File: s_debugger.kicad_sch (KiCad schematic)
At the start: 34 parts, among them J4 USB_C_Receptacle, Q1 S9013, U2 XC6206PxxxMR

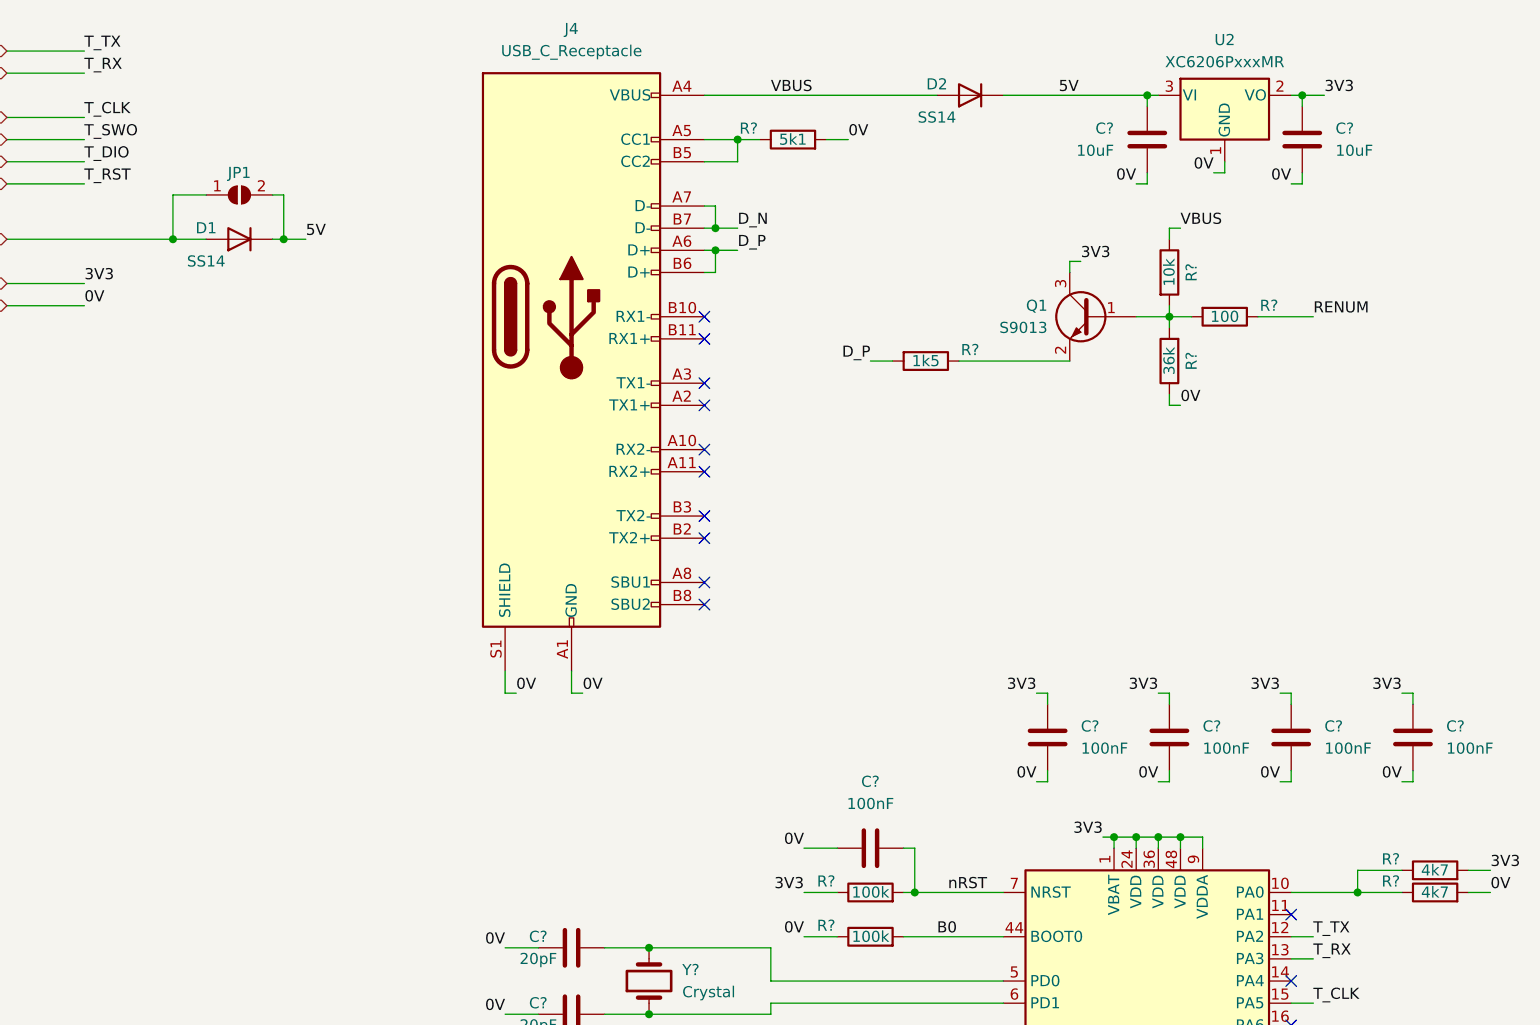
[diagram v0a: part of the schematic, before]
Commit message: passif en 0402
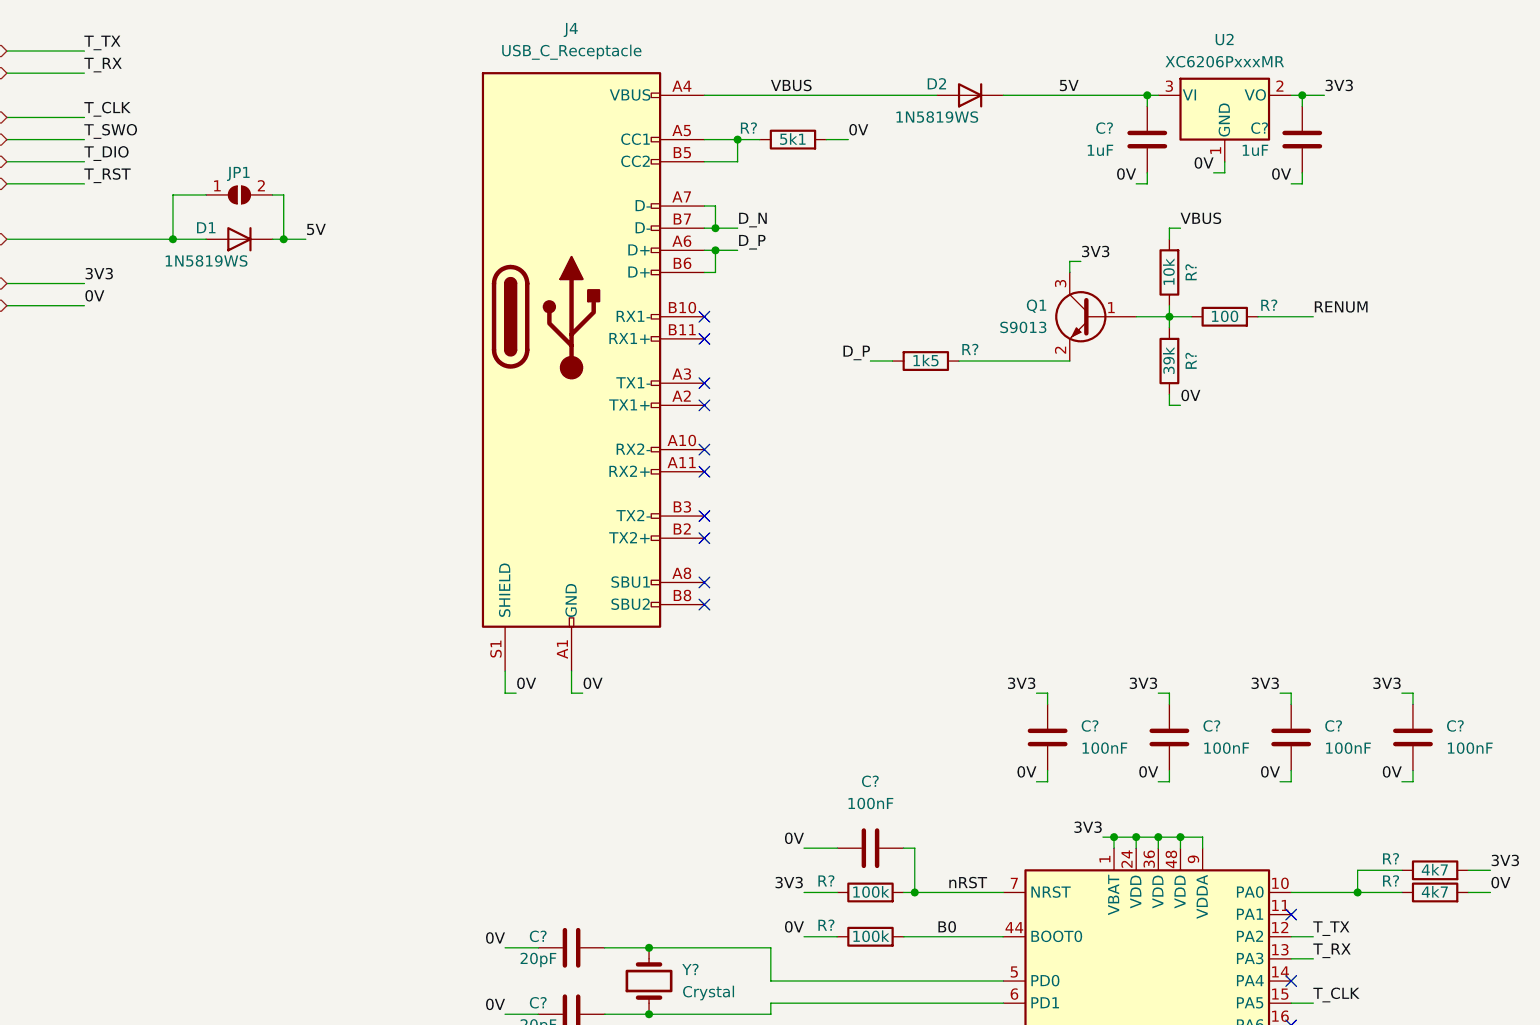
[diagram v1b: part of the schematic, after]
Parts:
- removed C? (x5): 100nF, Capacitor_SMD:C_0603_1608Metric, symbol Device:C
- removed C?: 10uF, Capacitor_SMD:C_0805_2012Metric, symbol Device:C
- removed C?: 20pF, Capacitor_SMD:C_0603_1608Metric, symbol Device:C
- removed R? (x2): 100k, Resistor_SMD:R_0603_1608Metric, symbol Device:R
- removed R? (x2): 10k, Resistor_SMD:R_0603_1608Metric, symbol Device:R
- removed R?: 100, Resistor_SMD:R_0603_1608Metric, symbol Device:R
- removed R?: 4k7, Resistor_SMD:R_0603_1608Metric, symbol Device:R
- added C? (x5): 100nF, Capacitor_SMD:C_0402_1005Metric, symbol Device:C
- added C?: 1uF, Capacitor_SMD:C_0402_1005Metric, symbol Device:C
- added C?: 20pF, Capacitor_SMD:C_0402_1005Metric, symbol Device:C
- added R? (x2): 10k, Resistor_SMD:R_0402_1005Metric, symbol Device:R
- added R? (x2): 100k, Resistor_SMD:R_0402_1005Metric, symbol Device:R
- added R?: 4k7, Resistor_SMD:R_0402_1005Metric, symbol Device:R
- added R?: 100, Resistor_SMD:R_0402_1005Metric, symbol Device:R
- C?: value 10uF -> 1uF; footprint Capacitor_SMD:C_0805_2012Metric -> Capacitor_SMD:C_0402_1005Metric; LCSC C15850 -> C52923
- C?: footprint Capacitor_SMD:C_0603_1608Metric -> Capacitor_SMD:C_0402_1005Metric; LCSC C1648 -> C1554
- D1, D2: value SS14 -> 1N5819WS; footprint Diode_SMD:D_SMA -> Diode_SMD:D_SOD-323; LCSC C2480 -> C191023
- R?: value 36k -> 39k; footprint Resistor_SMD:R_0603_1608Metric -> Resistor_SMD:R_0402_1005Metric; LCSC C23147 -> C25783
- R? (x2): footprint Resistor_SMD:R_0603_1608Metric -> Resistor_SMD:R_0402_1005Metric; LCSC C22962 -> C25091
- R?: footprint Resistor_SMD:R_0603_1608Metric -> Resistor_SMD:R_0402_1005Metric; LCSC C22843 -> C25867
- R?: footprint Resistor_SMD:R_0603_1608Metric -> Resistor_SMD:R_0402_1005Metric; LCSC C22775 -> C25076
- R?: footprint Resistor_SMD:R_0603_1608Metric -> Resistor_SMD:R_0402_1005Metric; LCSC C25804 -> C25744
- R?: footprint Resistor_SMD:R_0603_1608Metric -> Resistor_SMD:R_0402_1005Metric; LCSC C23162 -> C25900
- R?: footprint Resistor_SMD:R_0603_1608Metric -> Resistor_SMD:R_0402_1005Metric; LCSC C23186 -> C25905
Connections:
- net 0V: now also C?.1, C?.1, C?.1, C?.1, C?.1, C?.1, C?.2, R?.1, R?.1, R?.2
- net 3V3: now also C?.2, C?.2, C?.2, C?.2, C?.2, R?.1
- net B0: now also R?.2
- net RENUM: now also R?.2
- net VBUS: now also R?.2
- net nRST: now also C?.1, R?.2
- net at U?.6 (PD1), Y?.1: now also C?.2
- net at Q1.1 (B), R?.2: now also R?.1, R?.1
- net at R?.1, U?.10 (PA0): now also R?.1
- net at U?.3 (PC14): now also R?.2

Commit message: simplification
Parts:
- removed C? (x5): 100nF, Capacitor_SMD:C_0402_1005Metric, symbol Device:C
- removed C? (x2): 20pF, Capacitor_SMD:C_0402_1005Metric, symbol Device:C
- removed D2: 1N5819WS, Diode_SMD:D_SOD-323, symbol Device:D
- removed D?: KT-0603R, LED_SMD:LED_0603_1608Metric, symbol Device:LED
- removed D?: 19-217/BHC-ZL1M2RY/6T, LED_SMD:LED_0603_1608Metric, symbol Device:LED
- removed J4: USB_C_Receptacle, Connector_USB:USB_C_Receptacle_G-Switch_GT-USB-7010ASV, symbol Connector:USB_C_Receptacle
- removed J?: Conn_ARM_SWD_TagConnect_TC2030-NL, Connector:Tag-Connect_TC2030-IDC-NL_2x03_P1.27mm_Vertical, symbol Connector:Conn_ARM_SWD_TagConnect_TC2030-NL
- removed JP1: SolderJumper_2_Open, Jumper:SolderJumper-2_P1.3mm_Open_TrianglePad1.0x1.5mm, symbol Jumper:SolderJumper_2_Open
- removed Q1: S9013, Package_TO_SOT_SMD:SOT-23, symbol Transistor_BJT:BC817
- removed R?: 39k, Resistor_SMD:R_0402_1005Metric, symbol Device:R
- removed R? (x3): 10k, Resistor_SMD:R_0402_1005Metric, symbol Device:R
- removed R? (x2): 100k, Resistor_SMD:R_0402_1005Metric, symbol Device:R
- removed R? (x2): 4k7, Resistor_SMD:R_0402_1005Metric, symbol Device:R
- removed R? (x2): 220, Resistor_SMD:R_0402_1005Metric, symbol Device:R
- removed R?: 1k5, Resistor_SMD:R_0402_1005Metric, symbol Device:R
- removed R? (x2): 100, Resistor_SMD:R_0402_1005Metric, symbol Device:R
- removed R?: 5k1, Resistor_SMD:R_0402_1005Metric, symbol Device:R
- removed U?: STM32F103CBTx, Package_QFP:LQFP-48_7x7mm_P0.5mm, symbol MCU_ST_STM32F1:STM32F103CBTx
- removed Y?: Crystal, Crystal:Crystal_SMD_5032-2Pin_5.0x3.2mm, symbol Device:Crystal
- added J3: Conn_02x05_Top_Bottom, Connector_PinSocket_2.00mm:PinSocket_2x05_P2.00mm_Horizontal, symbol Connector_Generic:Conn_02x05_Top_Bottom
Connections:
- net 0V: now also J3.6 (Pin_6)
- net 3V3: now also J3.10 (Pin_10)
- net T_CLK: now also J3.4 (Pin_4)
- net T_DIO: now also J3.3 (Pin_3)
- net T_RST: now also J3.9 (Pin_9)
- net T_RX: now also J3.7 (Pin_7)
- net T_SWO: now also J3.5 (Pin_5)
- net T_TX: now also J3.8 (Pin_8)
- no-connect marks 29 -> 2
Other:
- note removed: "led bleue"
- note removed: "led rouge"
- note removed: "ne pas braser sur PC14"
- moved on the sheet: C?, U2

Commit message: renumerotation
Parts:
- renumbered U2 to U1
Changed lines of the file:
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@@
         )
         (path "/df3b256b-8149-4d05-9297-21d9891015ed/16240612-d267-452a-8e47-9f10a80c98e1"
-          (reference "C8") (unit 1)
+          (reference "C2") (unit 1)
         )
       )
@@
         )
         (path "/df3b256b-8149-4d05-9297-21d9891015ed/16240612-d267-452a-8e47-9f10a80c98e1"
-          (reference "C5") (unit 1)
+          (reference "C1") (unit 1)
         )
       )
@@
   (symbol (lib_id "Regulator_Linear:XC6206PxxxMR") (at 80.01 38.1 0) (unit 1)
     (in_bom yes) (on_board yes) (dnp no) (fields_autoplaced)
-    (property "Reference" "U2" (at 80.01 31.75 0)
+    (property "Reference" "U1" (at 80.01 31.75 0)
       (effects (font (size 1.27 1.27)))
     )
@@
       (project "Ultrogothe"
         (path "/df3b256b-8149-4d05-9297-21d9891015ed/16240612-d267-452a-8e47-9f10a80c98e1"
-          (reference "U2") (unit 1)
+          (reference "U1") (unit 1)
         )
       )

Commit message: routage fini
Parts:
- removed J3: Conn_02x05_Top_Bottom, Connector_PinSocket_2.00mm:PinSocket_2x05_P2.00mm_Horizontal, symbol Connector_Generic:Conn_02x05_Top_Bottom
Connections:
- no-connect marks 2 -> 0
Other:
- moved on the sheet: C?, D1, U1

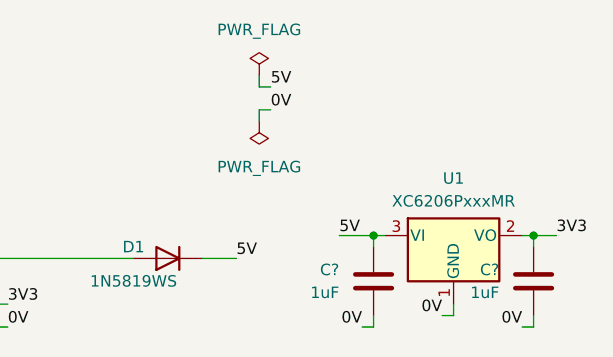
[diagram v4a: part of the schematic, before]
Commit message: Passage à kicad 8
et correction des chemins spécifiques
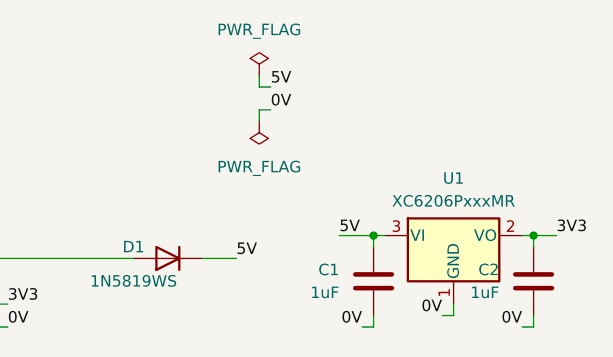
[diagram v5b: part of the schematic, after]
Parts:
- gave numbers to parts that had none: 2
